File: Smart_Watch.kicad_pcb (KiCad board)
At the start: 4 copper layers, 32 x 31.3 mm, 61 parts, among them J1 2169900001, J2 Conn_01x02, J3 Conn_01x06, J4 Conn_01x02, SW2 SW_Push, SW3 SW_Push, SW4 SW_Push, SW5 SW_Push, SW6 SW_Push, SW7 SW_Push, U1 BMI270, U12 DRV2603RUNR, U2 OPT3004DNPR, U3 NORA-B106-00B, U4 LPS22DF, U5 W25Q32JVSS, U6 NPM1300-QEAA-R7, U7 FAN5622SX, U8 ESDR0502NMUTBG, U9 MAX30102EFD_T, X1 Q13FC1350000400, X608 Display

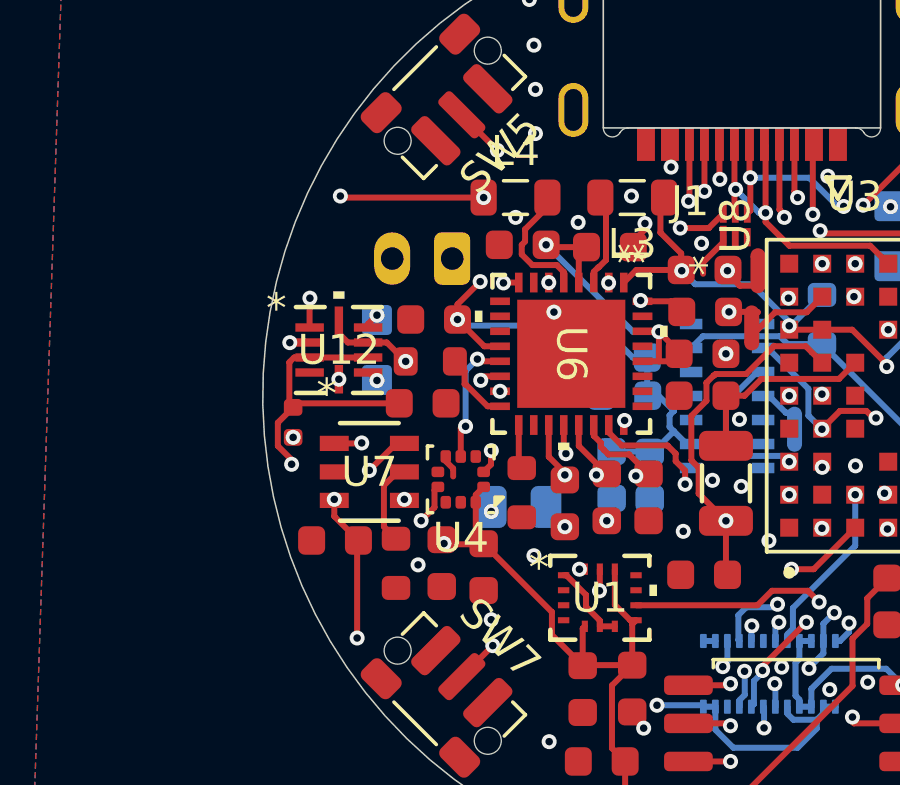
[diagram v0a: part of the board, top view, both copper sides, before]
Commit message: Everything but ZIF moved
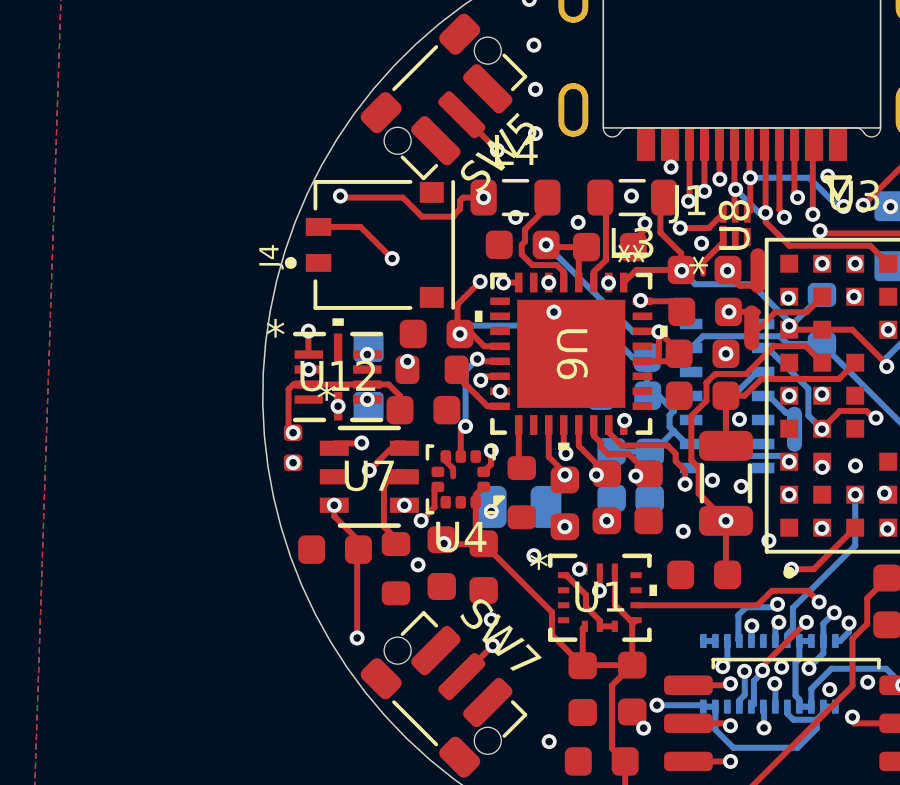
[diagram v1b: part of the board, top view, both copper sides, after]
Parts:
- J4: footprint Connector_JST:JST_PH_S2B-PH-K_1x02_P2.00mm_Horizontal -> Smart_Watch:MOLEX_0781710002; moved to F.Cu
- moved J2 0.94 mm to (159.7, 107.2)
- moved U12 0.90 mm to (158.7, 107.2)
- moved R9 0.85 mm to (157.2, 109.6)
- moved J4 0.82 mm to (161.8, 102.8), turned to 90 degrees
- moved C15 0.49 mm to (161.9, 105.8)
- moved C14 0.30 mm to (158.6, 113.0)
- moved R13 0.29 mm to (161.8, 107.0)
- moved C23 0.23 mm to (161.5, 108.3)
- moved R11 0.18 mm to (160.6, 113.6)
- moved U7 0.16 mm to (159.7, 110.6)
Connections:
- U2 pad V: GND -> (no net)
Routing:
- net VSYS: track 39.6 -> 35.6 mm
- net GND: track 22.3 -> 19.2 mm
- net +BATT: track 15.8 -> 18.7 mm, vias 2 -> 3
- net +3V0: track 50.3 -> 51.2 mm
- net /Architecture/MCU/LRA_EN: track 27.1 -> 27.8 mm
- net /Architecture/MCU/LRA_PWM: track 25.6 -> 25.0 mm
- net /Architecture/Peripherals/MOTOR+: track 0.53 -> 0.00 mm

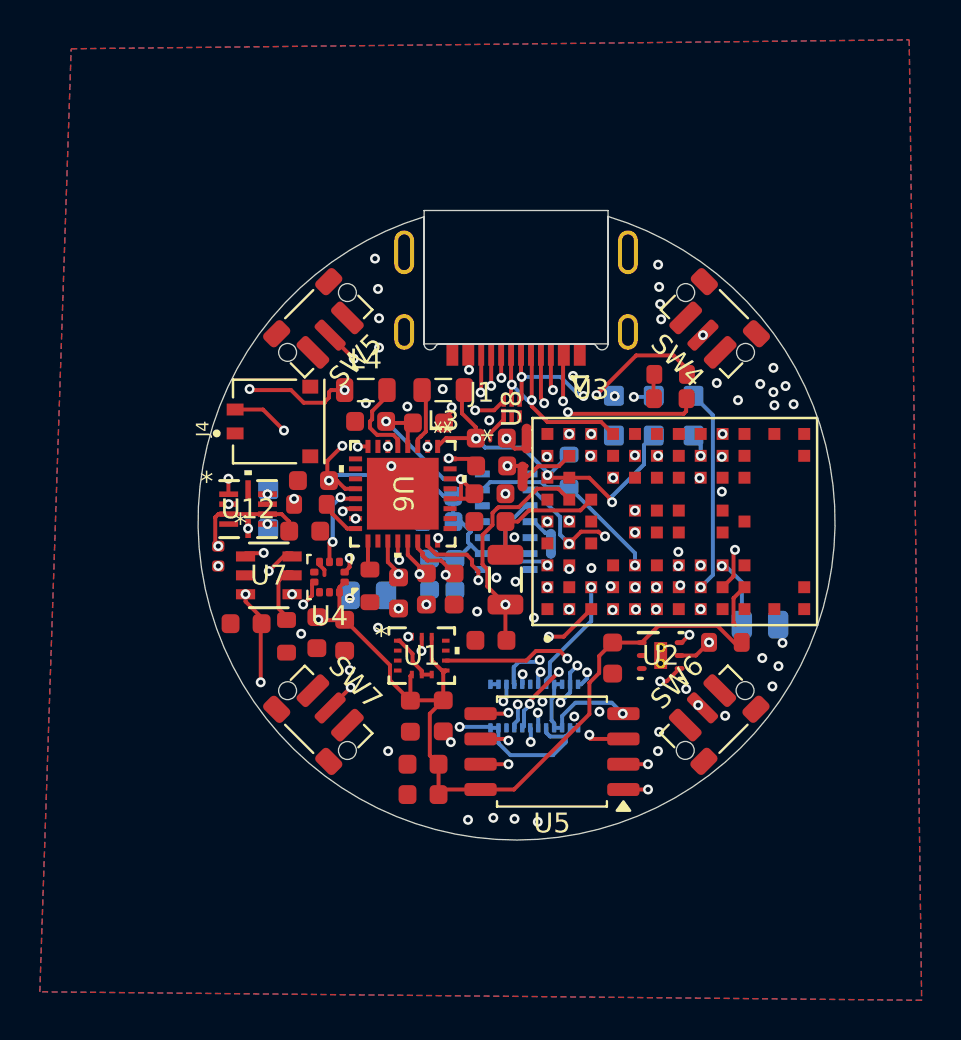
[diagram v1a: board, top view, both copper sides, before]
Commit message: Everything Moved to Front
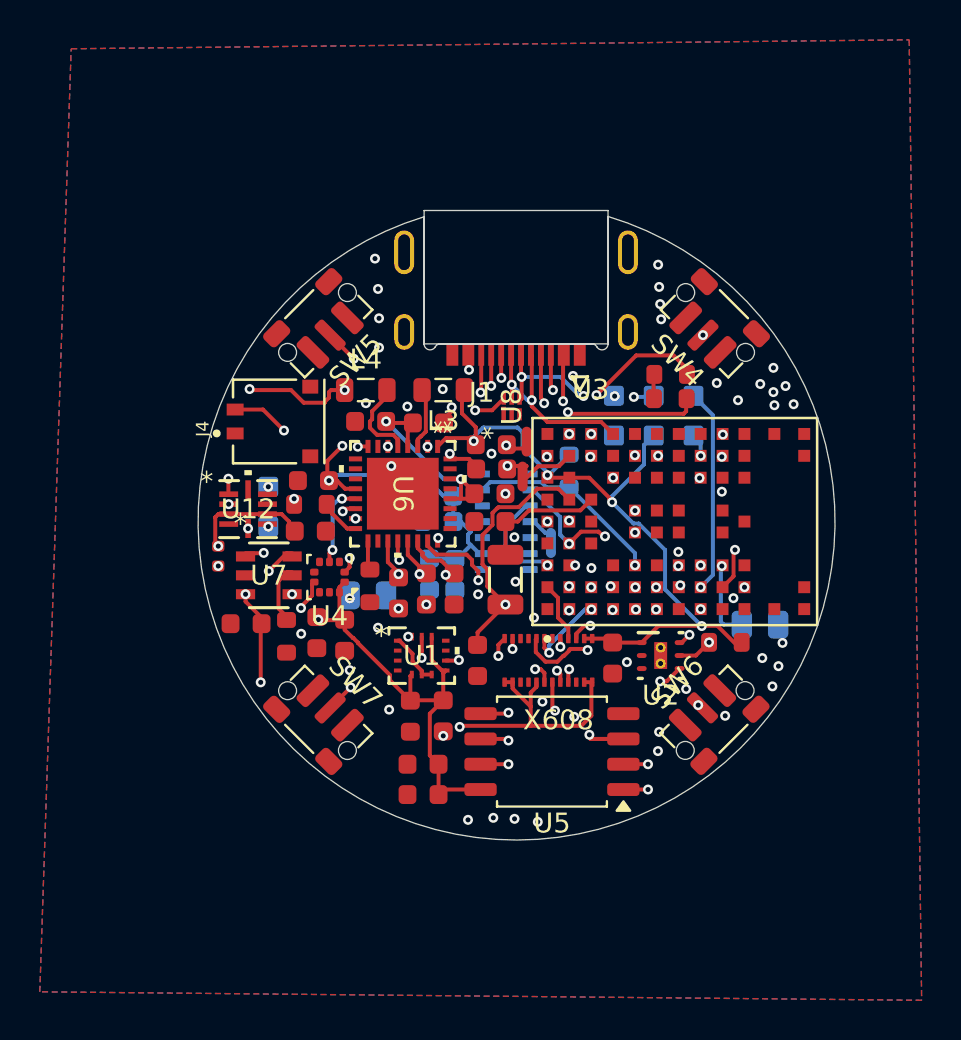
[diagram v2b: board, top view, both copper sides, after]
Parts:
- X608: moved to F.Cu
- moved X608 2.40 mm to (173.8, 114.8), turned to 0 degrees
- moved C24 1.21 mm to (170.2, 114.8), turned to 90 degrees
- moved C19 0.33 mm to (170.9, 104.0)
- moved C23 0.28 mm to (161.8, 108.3)
- moved C20 0.15 mm to (170.9, 105.2)
- moved NT1 0.15 mm to (172.7, 103.8)
- moved J2 0.12 mm to (159.7, 107.1)
- moved U8 0.10 mm to (171.9, 102.1)
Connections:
- X608 pad 11: 1V8 -> +1V8
- X608 pad 12: 1V8 -> +1V8
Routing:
- net GND: track 19.2 -> 7.06 mm, vias 35 -> 36
- net /Architecture/MCU/DISPLAY_RST: track 28.4 -> 17.5 mm
- net /Architecture/MCU/CTP_INT: track 11.6 -> 3.62 mm, vias 3 -> 2
- net /Architecture/MCU/LEDK2: track 19.4 -> 13.6 mm, vias 4 -> 3
- net /Architecture/MCU/DISPLAY_CLK: track 10.5 -> 5.17 mm, vias 3 -> 2
- net +3V0: track 51.2 -> 55.3 mm
- net /Architecture/MCU/DISPLAY_CS: track 6.19 -> 3.01 mm, vias 2 -> 0
- net /Architecture/MCU/SDA: track 73.4 -> 71.4 mm
- net /Architecture/MCU/QSPI_IO2: track 8.64 -> 10.4 mm
- net /Architecture/MCU/CTP_RST: track 18.2 -> 16.4 mm
- net /Architecture/MCU/SCL: track 61.0 -> 59.4 mm, vias 10 -> 9
- net /Architecture/MCU/DISPLAY_DC: track 5.81 -> 7.38 mm, vias 1 -> 2
- net /Architecture/MCU/DISPLAY_DATA: track 5.31 -> 4.07 mm
- net /Architecture/MCU/PMIC_INT: track 26.6 -> 27.6 mm
- net /Architecture/MCU/CLK2: track 17.0 -> 17.8 mm
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
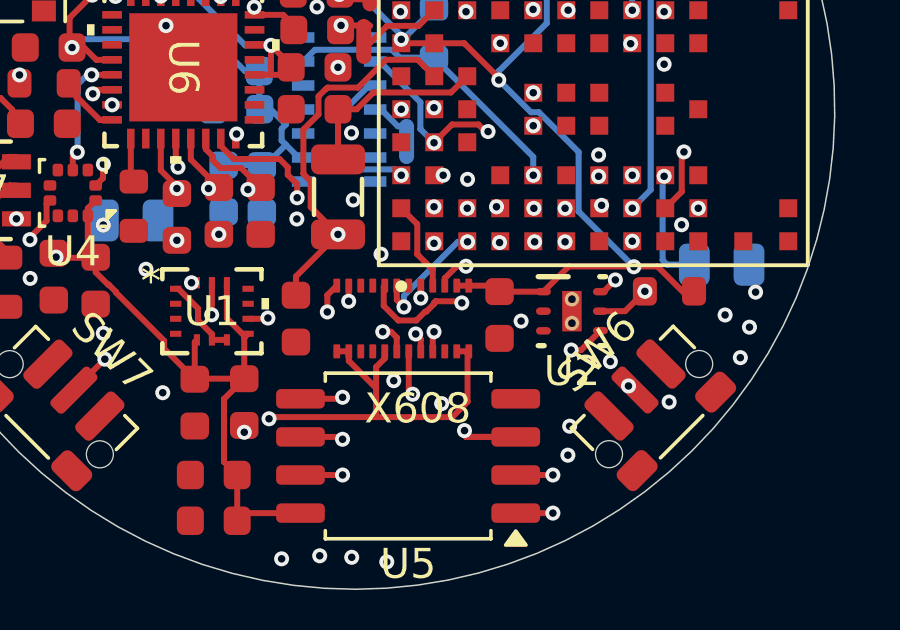
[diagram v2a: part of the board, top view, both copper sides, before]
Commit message: Updated ZIF Keepout & Cleaned Trace Routing
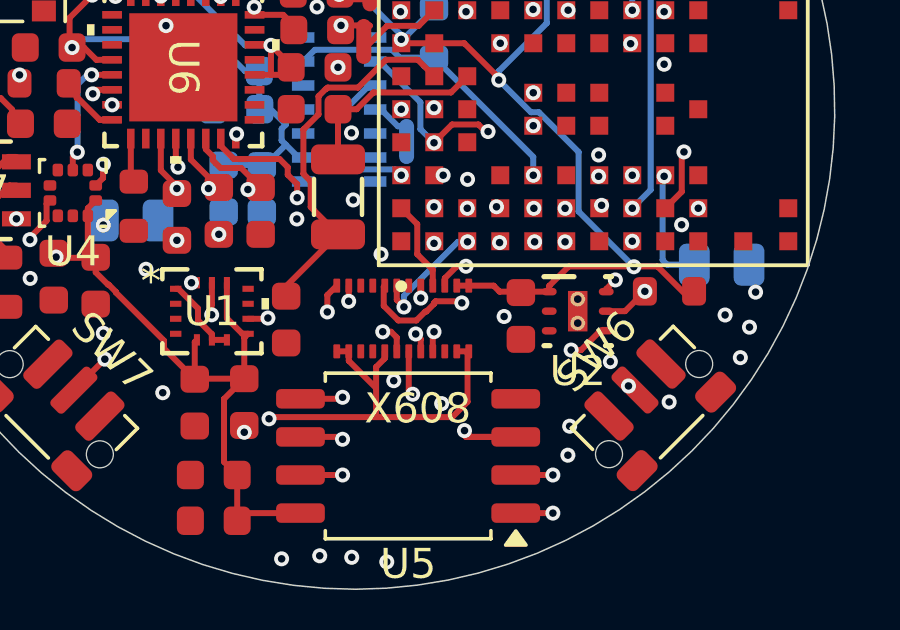
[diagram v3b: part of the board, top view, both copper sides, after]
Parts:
- moved C7 0.71 mm to (177.7, 114.7)
- moved C24 0.33 mm to (169.9, 114.9)
- moved U2 0.19 mm to (179.6, 114.6)
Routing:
- net /Architecture/MCU/CLK2: track 17.8 -> 12.7 mm, vias 1 -> 0
- net /Architecture/MCU/LEDK1: track 25.0 -> 23.6 mm
- net /Architecture/MCU/PMIC_INT: track 27.6 -> 26.9 mm

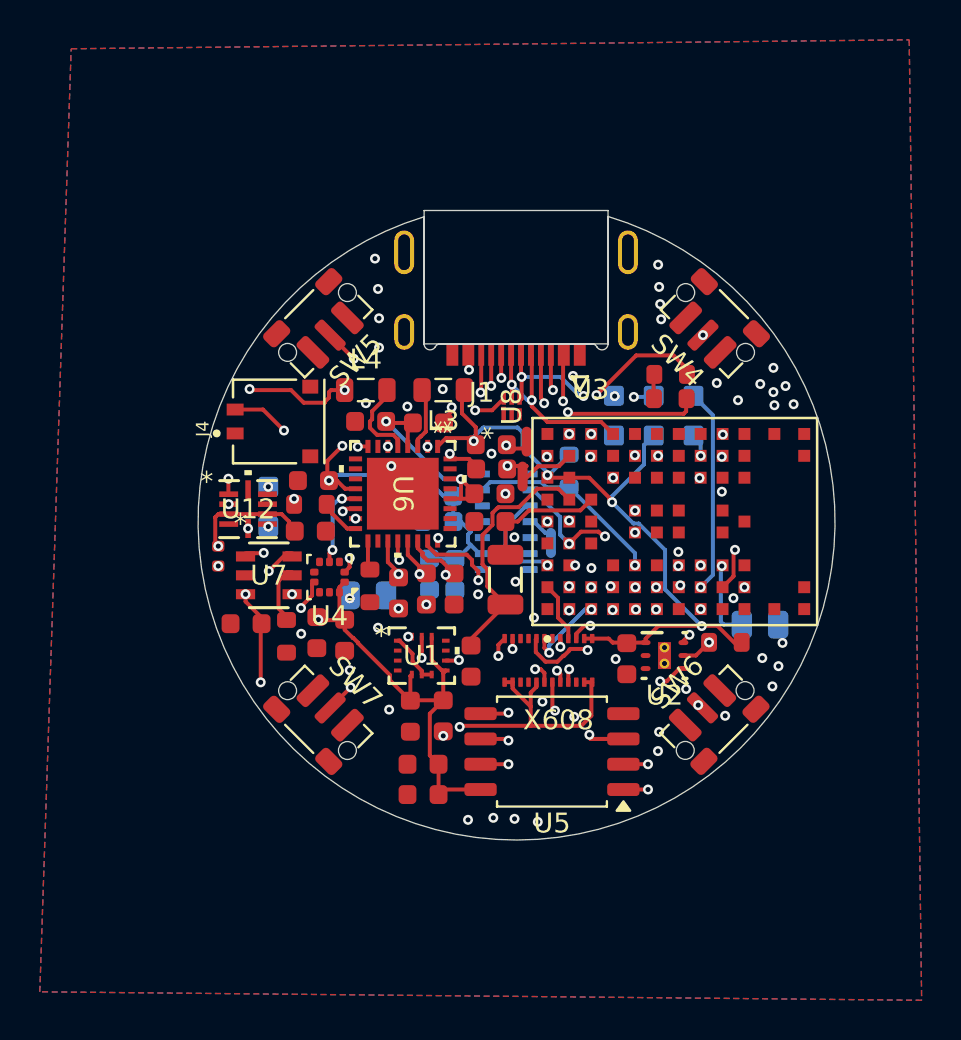
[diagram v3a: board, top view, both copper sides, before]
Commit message: Edited Switch & MCU Location to Fit Case
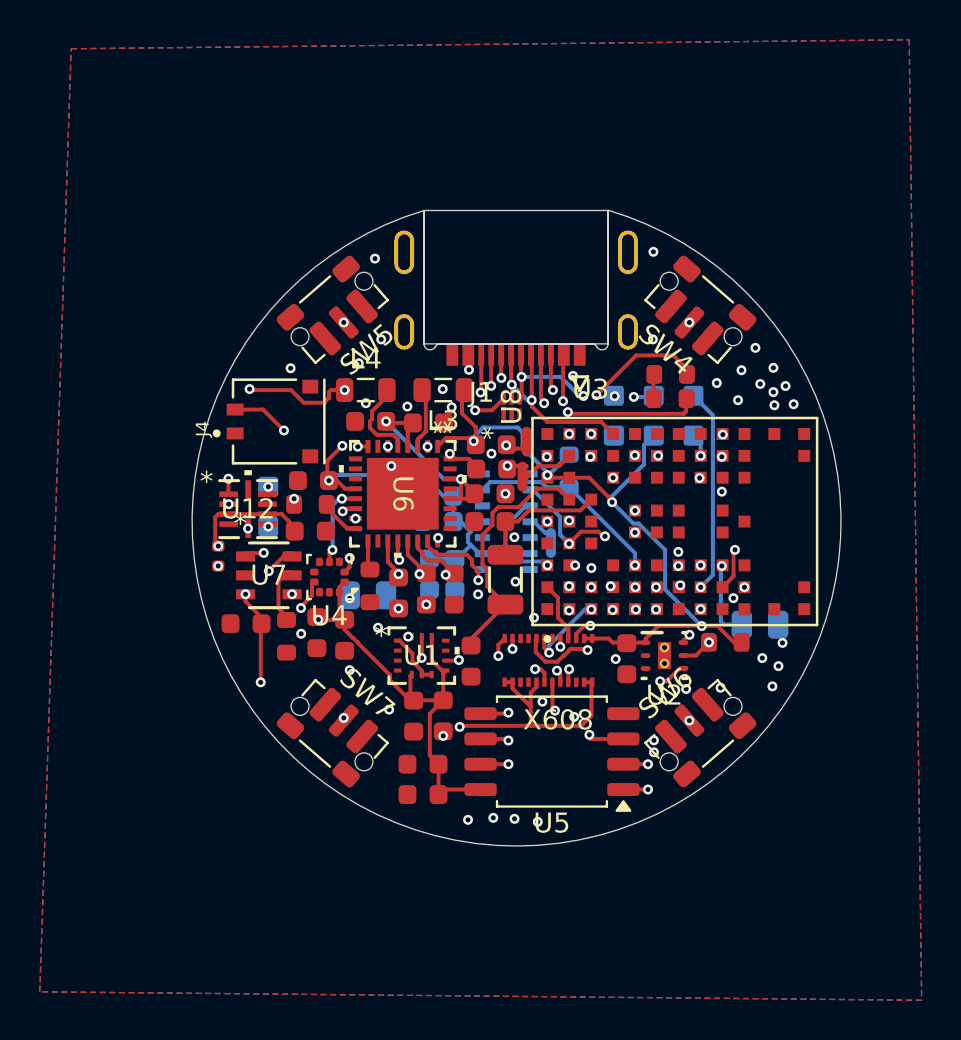
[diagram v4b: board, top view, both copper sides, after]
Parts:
- moved SW4 1.00 mm to (181.4, 97.2), turned to 139.037 degrees
- moved SW7 1.00 mm to (162.9, 118.5), turned to -40.963 degrees
- moved SW5 1.00 mm to (162.9, 97.2), turned to -139.037 degrees
- moved SW6 0.98 mm to (181.4, 118.5), turned to 40.963 degrees
- moved C5 0.16 mm to (167.0, 117.6)
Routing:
- net /Architecture/MCU/SDA: track 71.3 -> 72.4 mm
- net /Architecture/MCU/BTN_1: track 13.0 -> 14.0 mm
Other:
- board size 32 x 31.3 mm -> 32.6 x 31.9 mm

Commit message: Added Test Points and Changed to Top Mounted USBC
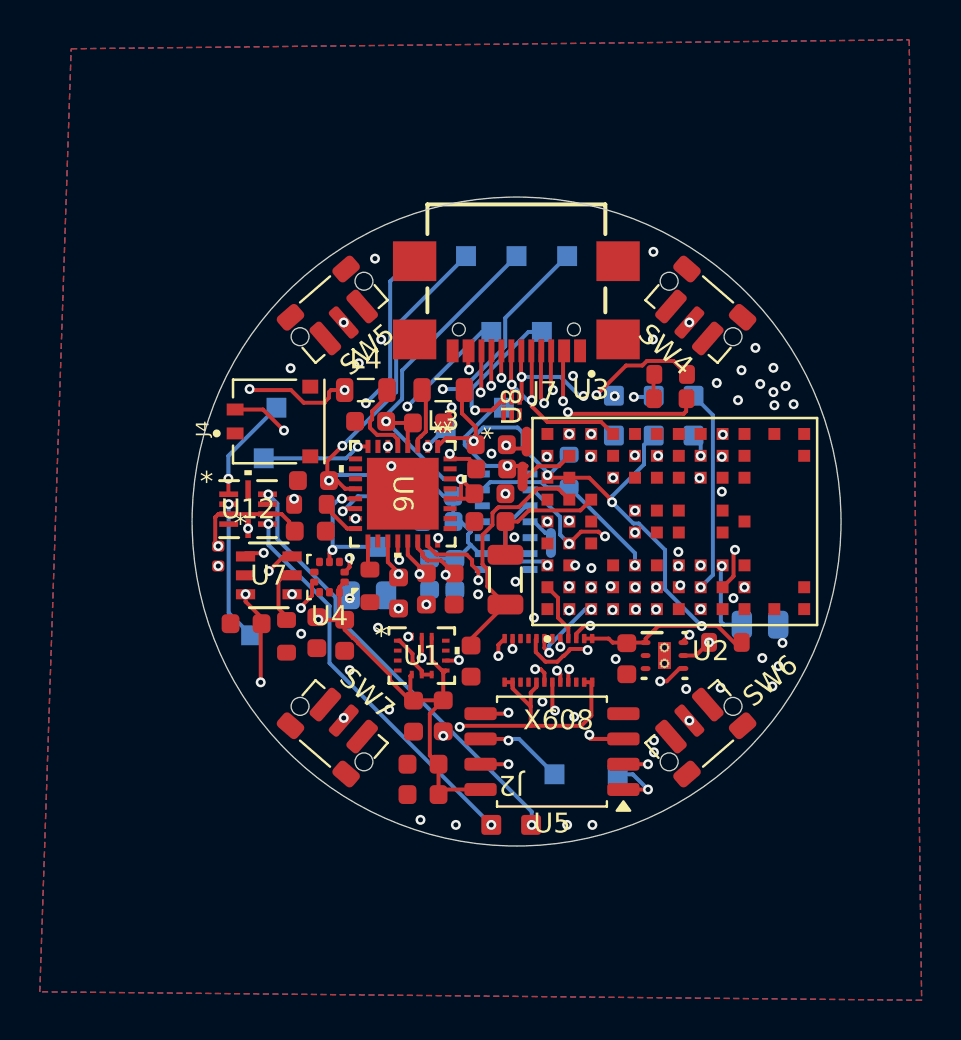
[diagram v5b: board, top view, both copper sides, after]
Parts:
- removed J1: 2169900001, Smart_Watch:MOLEX_2169900001
- added 1V8: TestPoint, TestPoint:TestPoint_Pad_1.0x1.0mm, B.Cu at (169.6, 94.5)
- added 3V0: TestPoint, TestPoint:TestPoint_Pad_1.0x1.0mm, B.Cu at (174.7, 94.5)
- added BATT: TestPoint, TestPoint:TestPoint_Pad_1.0x1.0mm, B.Cu at (167.1, 94.5)
- added GND: TestPoint, TestPoint:TestPoint_Pad_1.0x1.0mm, B.Cu at (177.2, 98.3)
- added J7: USB4110GFA, Smart_Watch:GCT_USB4110GFA, F.Cu at (172.1, 98.2)
- added LRA_EN: TestPoint, TestPoint:TestPoint_Pad_1.0x1.0mm, B.Cu at (160.1, 102.1)
- added LRA_PWM: TestPoint, TestPoint:TestPoint_Pad_1.0x1.0mm, B.Cu at (158.8, 113.6)
- added PMIC_INT: TestPoint, TestPoint:TestPoint_Pad_1.0x1.0mm, B.Cu at (159.4, 104.7)
- added QSPI_CLK: TestPoint, TestPoint:TestPoint_Pad_1.0x1.0mm, B.Cu at (174.1, 120.5)
- added QSPI_CS: TestPoint, TestPoint:TestPoint_Pad_1.0x1.0mm, B.Cu at (177.2, 120.5)
- added SCL: TestPoint, TestPoint:TestPoint_Pad_1.0x1.0mm, B.Cu at (165.2, 106.6)
- added SDA: TestPoint, TestPoint:TestPoint_Pad_1.0x1.0mm, B.Cu at (165.2, 109.1)
- added TP15: TestPoint, TestPoint:TestPoint_Pad_1.0x1.0mm, B.Cu at (168.6, 103.2)
- added TP16: TestPoint, TestPoint:TestPoint_Pad_1.0x1.0mm, B.Cu at (171.5, 102.1)
- added VBUS_IN: TestPoint, TestPoint:TestPoint_Pad_1.0x1.0mm, B.Cu at (173.4, 98.3)
- added VBUS_OUT: TestPoint, TestPoint:TestPoint_Pad_1.0x1.0mm, B.Cu at (170.9, 98.3)
- added VSYS: TestPoint, TestPoint:TestPoint_Pad_1.0x1.0mm, B.Cu at (172.2, 94.5)
- J2: moved to F.Cu
- moved J2 20.1 mm to (171.9, 123.1), turned to 180 degrees
- moved G*** 10.2 mm to (181.1, 99.9)
- moved G*** 3.53 mm to (167.2, 117.8)
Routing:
- net /Architecture/Peripherals/MOTOR+: track 0.00 -> 22.1 mm, vias 1 -> 2
- net /Architecture/Peripherals/MOTOR-: track 0.00 -> 19.8 mm, vias 1 -> 2
- net +1V8: track 92.3 -> 104.4 mm
- net VSYS: track 35.6 -> 46.6 mm
- net +3V0: track 55.3 -> 65.2 mm
- net +BATT: track 18.7 -> 27.1 mm
- net /Architecture/MCU/LRA_PWM: track 25.0 -> 32.0 mm
- net /Architecture/MCU/VBUS_IN: track 24.0 -> 29.9 mm
- net /Architecture/MCU/VBUS_OUT: track 23.2 -> 28.9 mm
- net PGND2: track 7.40 -> 12.9 mm
- net /Architecture/MCU/PMIC_INT: track 26.9 -> 31.9 mm
- net /Architecture/MCU/LRA_EN: track 27.5 -> 32.1 mm
- net /Architecture/MCU/QSPI_CLK: track 15.7 -> 18.8 mm
- net /Architecture/MCU/SDA: track 72.4 -> 74.7 mm
- net /Architecture/MCU/SCL: track 59.6 -> 61.6 mm
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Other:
- board size 32.6 x 31.9 mm -> 32.6 x 32.6 mm

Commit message: Small Updates
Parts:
- moved J7 0.29 mm to (172.1, 97.9)
- renumbered LRA_EN to TP1, 3V0 to TP10, 1V8 to TP11, VSYS to TP12, PMIC_INT to TP13, GND to TP14, LRA_PWM to TP2, QSPI_CLK to TP3, QSPI_CS to TP4, SDA to TP5, SCL to TP6, BATT to TP7, VBUS_IN to TP8, VBUS_OUT to TP9
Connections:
- R1 pad 1: VDD -> +1V8
- R2 pad 1: VDD -> +1V8
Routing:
- net /Architecture/MCU/LEDK1: track 23.6 -> 17.1 mm, vias 4 -> 3
- net +1V8: track 104.4 -> 109.8 mm, vias 7 -> 8
- net GND: track 7.06 -> 8.61 mm
- net VDD: track 1.52 -> 0.00 mm
